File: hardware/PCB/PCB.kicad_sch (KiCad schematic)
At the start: 13 parts, among them J1 Conn_01x02, J10 Conn_01x06_Socket, J11 Conn_01x03_Socket, J12 Conn_01x03_Socket, J13 Conn_01x03_Socket, J2 Conn_01x04, J3 Conn_01x19, J4 Conn_01x19, J5 Conn_01x02, J6 Conn_01x02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

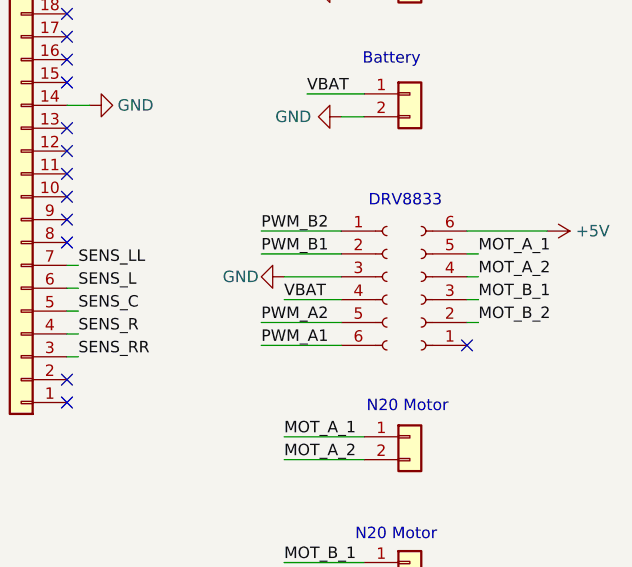
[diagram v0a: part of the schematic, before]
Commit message: Update PCB design with correct measurements.
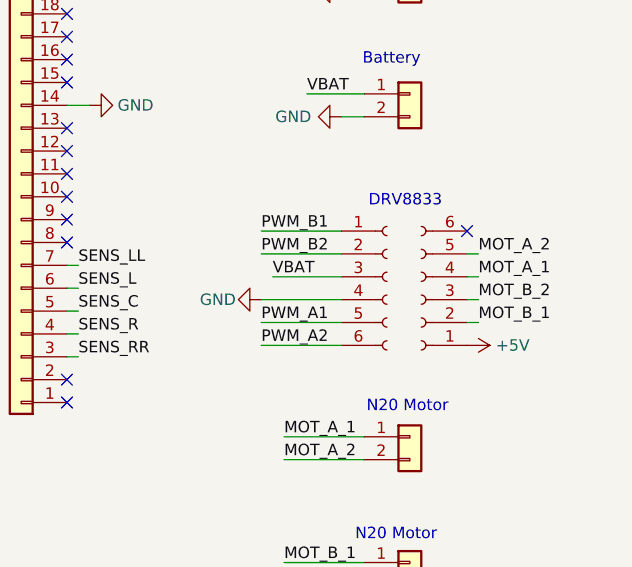
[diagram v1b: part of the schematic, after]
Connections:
- net +5V: now also J10.1 (Pin_1); no longer J10.6 (Pin_6)
- net GND: now also J9.4 (Pin_4); no longer J9.3 (Pin_3)
- net MOT_A_1: now also J10.4 (Pin_4); no longer J10.5 (Pin_5)
- net MOT_A_2: now also J10.5 (Pin_5); no longer J10.4 (Pin_4)
- net MOT_B_1: now also J10.2 (Pin_2); no longer J10.3 (Pin_3)
- net MOT_B_2: now also J10.3 (Pin_3); no longer J10.2 (Pin_2)
- net PWM_A1: now also J9.5 (Pin_5); no longer J9.6 (Pin_6)
- net PWM_A2: now also J9.6 (Pin_6); no longer J9.5 (Pin_5)
- net PWM_B1: now also J9.1 (Pin_1); no longer J9.2 (Pin_2)
- net PWM_B2: now also J9.2 (Pin_2); no longer J9.1 (Pin_1)
- net VBAT: now also J9.3 (Pin_3); no longer J9.4 (Pin_4)
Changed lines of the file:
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@@
+	)
+	(no_connect
+		(at 194.31 88.9)
 	)
 	(no_connect
@@
 	)
 	(no_connect
-		(at 194.31 101.6)
-	)
-	(no_connect
 		(at 133.35 105.41)
 	)
@@
 	(wire
 		(pts
-			(xy 194.31 88.9) (xy 203.2 88.9)
-		)
-		(stroke
-			(width 0)
-			(type default)
-		)
-	)
-	(wire
-		(pts
 			(xy 173.99 114.3) (xy 182.88 114.3)
 		)
@@
 	(wire
 		(pts
-			(xy 173.99 96.52) (xy 180.34 96.52)
+			(xy 172.72 93.98) (xy 180.34 93.98)
 		)
 		(stroke
@@
 	(wire
 		(pts
+			(xy 171.45 96.52) (xy 180.34 96.52)
+		)
+		(stroke
+			(width 0)
+			(type default)
+		)
+	)
+	(wire
+		(pts
 			(xy 102.87 111.76) (xy 105.41 111.76)
 		)
@@
 		(pts
 			(xy 151.13 102.87) (xy 149.86 102.87)
-		)
-		(stroke
-			(width 0)
-			(type default)
-		)
-	)
-	(wire
-		(pts
-			(xy 173.99 93.98) (xy 180.34 93.98)
 		)
 		(stroke
@@
 		)
 	)
+	(label "PWM_A2"
+		(at 171.45 101.6 0)
+		(effects
+			(font
+				(size 1.27 1.27)
+			)
+			(justify left bottom)
+		)
+	)
 	(label "PWM_A1"
-		(at 171.45 101.6 0)
-		(effects
-			(font
-				(size 1.27 1.27)
-			)
-			(justify left bottom)
-		)
-	)
-	(label "PWM_A2"
 		(at 171.45 99.06 0)
 		(effects
@@
 		)
 	)
-	(label "PWM_B1"
+	(label "PWM_B2"
 		(at 171.45 91.44 0)
 		(effects
@@
 	)
 	(label "VBAT"
-		(at 173.99 96.52 0)
+		(at 172.72 93.98 0)
 		(effects
 			(font
@@
 		)
 	)
-	(label "PWM_B2"
+	(label "PWM_B1"
 		(at 171.45 88.9 0)
 		(effects
@@
 		)
 	)
-	(label "MOT_B_1"
+	(label "MOT_B_2"
 		(at 195.58 96.52 0)
 		(effects
@@
 		)
 	)
-	(label "MOT_A_1"
+	(label "MOT_A_2"
 		(at 195.58 91.44 0)
 		(effects
@@
 		)
 	)
-	(label "MOT_A_2"
+	(label "MOT_A_1"
 		(at 195.58 93.98 0)
 		(effects
@@
 		)
 	)
-	(label "MOT_B_2"
+	(label "MOT_B_1"
 		(at 195.58 99.06 0)
 		(effects
@@
 	(symbol
 		(lib_id "power:+5V")
-		(at 203.2 88.9 270)
+		(at 194.31 101.6 270)
 		(unit 1)
 		(body_style 1)
@@
 		(dnp no)
 		(property "Reference" "#PWR014"
-			(at 199.39 88.9 0)
+			(at 190.5 101.6 0)
 			(hide yes)
 			(show_name no)
@@
 		)
 		(property "Value" "+5V"
-			(at 208.28 88.9 90)
+			(at 199.39 101.6 90)
 			(show_name no)
 			(do_not_autoplace no)
@@
 		)
 		(property "Footprint" ""
-			(at 203.2 88.9 0)
+			(at 194.31 101.6 0)
 			(hide yes)
 			(show_name no)
@@
 		)
 		(property "Datasheet" ""
-			(at 203.2 88.9 0)
+			(at 194.31 101.6 0)
 			(hide yes)
 			(show_name no)
@@
 		)
 		(property "Description" "Power symbol creates a global label with name \"+5V\""
-			(at 203.2 88.9 0)
+			(at 194.31 101.6 0)
 			(hide yes)
 			(show_name no)
@@
 	(symbol
 		(lib_id "power:GND")
-		(at 173.99 93.98 270)
+		(at 171.45 96.52 270)
 		(unit 1)
 		(body_style 1)
@@
 		(dnp no)
 		(property "Reference" "#PWR02"
-			(at 167.64 93.98 0)
+			(at 165.1 96.52 0)
 			(hide yes)
 			(show_name no)
@@
 		)
 		(property "Value" "GND"
-			(at 169.164 93.98 90)
+			(at 166.624 96.52 90)
 			(show_name no)
 			(do_not_autoplace no)
@@
 		)
 		(property "Footprint" ""
-			(at 173.99 93.98 0)
+			(at 171.45 96.52 0)
 			(hide yes)
 			(show_name no)
@@
 		)
 		(property "Datasheet" ""
-			(at 173.99 93.98 0)
+			(at 171.45 96.52 0)
 			(hide yes)
 			(show_name no)
@@
 		)
 		(property "Description" "Power symbol creates a global label with name \"GND\" , ground"
-			(at 173.99 93.98 0)
-			(hide yes)
-			(show_name no)
+			(at 171.45 96.52 0)
+			(hide yes)
+			(show_name no)
